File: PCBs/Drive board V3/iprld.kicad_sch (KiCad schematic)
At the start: 39 parts, among them IC4 ADS1115IDGSR, J2 Conn_01x04_Pin, U15 AMS1117-3.3, U9 TCA9548APWR

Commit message: arm, drive and power modifications
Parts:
- added H1, H2, H3, H4: MountingHole, MountingHole:MountingHole_3.2mm_M3_Pad_TopBottom, symbol Mechanical:MountingHole
- added R1: 0R, Resistor_SMD:R_0805_2012Metric, symbol Device:R
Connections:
- net +3.3V: now also R1.1
- net GND: now also CONTROL_L2.6, CONTROL_R2.6
- net GNDPWR: no longer CONTROL_L2.6, CONTROL_R2.6
- net at U2.1 (3.3V): now also R1.2
- no-connect marks 28 -> 27

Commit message: i2c breakout correction, fuck you Maciej
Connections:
- net +3.3V: now also MRS_LB1.3 (Pin_3), MRS_LF1.3 (Pin_3), MRS_RB1.3 (Pin_3), MRS_RF1.3 (Pin_3); no longer MRS_LB1.1 (Pin_1), MRS_LF1.1 (Pin_1), MRS_RB1.1 (Pin_1), MRS_RF1.1 (Pin_1)
- net SCL_LB: now also MRS_LB1.1 (Pin_1); no longer MRS_LB1.2 (Pin_2)
- net SCL_LF: now also MRS_LF1.1 (Pin_1); no longer MRS_LF1.2 (Pin_2)
- net SCL_RB: now also MRS_RB1.1 (Pin_1); no longer MRS_RB1.2 (Pin_2)
- net SCL_RF: now also MRS_RF1.1 (Pin_1); no longer MRS_RF1.2 (Pin_2)
- net SDA_LB: now also MRS_LB1.2 (Pin_2); no longer MRS_LB1.3 (Pin_3)
- net SDA_LF: now also MRS_LF1.2 (Pin_2); no longer MRS_LF1.3 (Pin_3)
- net SDA_RB: now also MRS_RB1.2 (Pin_2); no longer MRS_RB1.3 (Pin_3)
- net SDA_RF: now also MRS_RF1.2 (Pin_2); no longer MRS_RF1.3 (Pin_3)
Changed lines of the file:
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@@
 	(wire
 		(pts
+			(xy 86.36 82.55) (xy 88.9 82.55)
+		)
+		(stroke
+			(width 0)
+			(type default)
+		)
+	)
+	(wire
+		(pts
 			(xy 295.91 139.7) (xy 306.07 139.7)
 		)
@@
 		)
 	)
-	(label "SCL_RB"
-		(at 90.17 110.49 180)
-		(effects
-			(font
-				(size 1.27 1.27)
-			)
-			(justify right bottom)
-		)
-	)
 	(label "SDA_RF"
 		(at 152.4 87.63 180)
@@
 		)
 	)
-	(label "SCL_RF"
-		(at 88.9 80.01 180)
-		(effects
-			(font
-				(size 1.27 1.27)
-			)
-			(justify right bottom)
-		)
-	)
 	(label "SDA"
 		(at 190.5 77.47 0)
@@
 		)
 	)
-	(label "SCL_LF"
-		(at 39.37 80.01 180)
+	(label "SDA_RB"
+		(at 90.17 110.49 180)
 		(effects
 			(font
@@
 		)
 	)
-	(label "SDA_RB"
-		(at 90.17 113.03 180)
-		(effects
-			(font
-				(size 1.27 1.27)
-			)
-			(justify right bottom)
-		)
-	)
 	(label "I_OUT_L"
 		(at 334.01 22.86 90)
@@
 		)
 	)
-	(label "IN2_L"
-		(at 72.39 260.35 0)
-		(effects
-			(font
-				(size 1.27 1.27)
-			)
-			(justify left bottom)
-		)
-	)
-	(label "D4"
-		(at 327.66 241.3 180)
+	(label "SCL_LF"
+		(at 39.37 77.47 180)
 		(effects
 			(font
@@
 		)
 	)
-	(label "SDA_RF"
-		(at 88.9 82.55 180)
+	(label "IN2_L"
+		(at 72.39 260.35 0)
 		(effects
 			(font
 				(size 1.27 1.27)
 			)
-			(justify right bottom)
+			(justify left bottom)
 		)
 	)
-	(label "SDA_LB"
-		(at 39.37 114.3 180)
+	(label "D4"
+		(at 327.66 241.3 180)
 		(effects
 			(font
@@
 		)
 	)
+	(label "SCL_RF"
+		(at 88.9 77.47 180)
+		(effects
+			(font
+				(size 1.27 1.27)
+			)
+			(justify right bottom)
+		)
+	)
 	(label "D5"
 		(at 219.71 228.6 0)
@@
 		)
 	)
+	(label "SCL_RB"
+		(at 90.17 107.95 180)
+		(effects
+			(font
+				(size 1.27 1.27)
+			)
+			(justify right bottom)
+		)
+	)
 	(label "EN_R"
 		(at 44.45 317.5 180)
@@
 		)
 	)
+	(label "SDA_RF"
+		(at 88.9 80.01 180)
+		(effects
+			(font
+				(size 1.27 1.27)
+			)
+			(justify right bottom)
+		)
+	)
 	(label "IN2_L"
 		(at 327.66 233.68 180)
@@
 		)
 	)
-	(label "SDA_LF"
-		(at 39.37 82.55 180)
-		(effects
-			(font
-				(size 1.27 1.27)
-			)
-			(justify right bottom)
-		)
-	)
 	(label "PWM_L"
 		(at 363.22 233.68 0)
@@
 		)
 	)
+	(label "SDA_LF"
+		(at 39.37 80.01 180)
+		(effects
+			(font
+				(size 1.27 1.27)
+			)
+			(justify right bottom)
+		)
+	)
 	(label "SDA_LB"
 		(at 152.4 82.55 180)
@@
 		)
 	)
+	(label "SCL_LB"
+		(at 39.37 109.22 180)
+		(effects
+			(font
+				(size 1.27 1.27)
+			)
+			(justify right bottom)
+		)
+	)
 	(label "SCL"
 		(at 363.22 218.44 0)
@@
 		)
 	)
-	(label "SCL_LB"
+	(label "SDA_LB"
 		(at 39.37 111.76 180)
 		(effects
@@
 	(symbol
 		(lib_id "power:+3.3V")
-		(at 90.17 107.95 0)
+		(at 90.17 113.03 90)
 		(unit 1)
 		(exclude_from_sim no)
@@
 		(fields_autoplaced yes)
 		(property "Reference" "#PWR076"
-			(at 90.17 111.76 0)
+			(at 93.98 113.03 0)
 			(effects
 				(font
@@
 		)
 		(property "Value" "+3.3V"
-			(at 90.17 102.87 0)
+			(at 88.9 110.49 90)
 			(effects
 				(font
@@
 		)
 		(property "Footprint" ""
-			(at 90.17 107.95 0)
+			(at 90.17 113.03 0)
 			(effects
 				(font
@@
 		)
 		(property "Datasheet" ""
-			(at 90.17 107.95 0)
+			(at 90.17 113.03 0)
 			(effects
 				(font
@@
 		)
 		(property "Description" "Power symbol creates a global label with name \"+3.3V\""
-			(at 90.17 107.95 0)
+			(at 90.17 113.03 0)
 			(effects
 				(font
@@
 	(symbol
 		(lib_id "power:+3.3V")
-		(at 39.37 109.22 0)
+		(at 39.37 114.3 90)
 		(unit 1)
 		(exclude_from_sim no)
@@
 		(fields_autoplaced yes)
 		(property "Reference" "#PWR0101"
-			(at 39.37 113.03 0)
+			(at 43.18 114.3 0)
 			(effects
 				(font
@@
 		)
 		(property "Value" "+3.3V"
-			(at 39.37 104.14 0)
+			(at 38.1 111.76 90)
 			(effects
 				(font
@@
 		)
 		(property "Footprint" ""
-			(at 39.37 109.22 0)
+			(at 39.37 114.3 0)
 			(effects
 				(font
@@
 		)
 		(property "Datasheet" ""
-			(at 39.37 109.22 0)
+			(at 39.37 114.3 0)
 			(effects
 				(font
@@
 		)
 		(property "Description" "Power symbol creates a global label with name \"+3.3V\""
-			(at 39.37 109.22 0)
+			(at 39.37 114.3 0)
 			(effects
 				(font
@@
 	(symbol
 		(lib_id "power:+3.3V")
-		(at 88.9 77.47 0)
+		(at 86.36 82.55 90)
 		(unit 1)
 		(exclude_from_sim no)
@@
 		(fields_autoplaced yes)
 		(property "Reference" "#PWR067"
-			(at 88.9 81.28 0)
+			(at 90.17 82.55 0)
 			(effects
 				(font
@@
 		)
 		(property "Value" "+3.3V"
-			(at 88.9 72.39 0)
+			(at 85.09 80.01 90)
 			(effects
 				(font
@@
 		)
 		(property "Footprint" ""
-			(at 88.9 77.47 0)
+			(at 86.36 82.55 0)
 			(effects
 				(font
@@
 		)
 		(property "Datasheet" ""
-			(at 88.9 77.47 0)
+			(at 86.36 82.55 0)
 			(effects
 				(font
@@
 		)
 		(property "Description" "Power symbol creates a global label with name \"+3.3V\""
-			(at 88.9 77.47 0)
+			(at 86.36 82.55 0)
 			(effects
 				(font
@@
 	(symbol
 		(lib_id "power:+3.3V")
-		(at 39.37 77.47 0)
+		(at 39.37 82.55 90)
 		(unit 1)
 		(exclude_from_sim no)
@@
 		(fields_autoplaced yes)
 		(property "Reference" "#PWR07"
-			(at 39.37 81.28 0)
+			(at 43.18 82.55 0)
 			(effects
 				(font
@@
 		)
 		(property "Value" "+3.3V"
-			(at 39.37 72.39 0)
+			(at 38.1 80.01 90)
 			(effects
 				(font
@@
 		)
 		(property "Footprint" ""
-			(at 39.37 77.47 0)
+			(at 39.37 82.55 0)
 			(effects
 				(font
@@
 		)
 		(property "Datasheet" ""
-			(at 39.37 77.47 0)
+			(at 39.37 82.55 0)
 			(effects
 				(font
@@
 		)
 		(property "Description" "Power symbol creates a global label with name \"+3.3V\""
-			(at 39.37 77.47 0)
+			(at 39.37 82.55 0)
 			(effects
 				(font

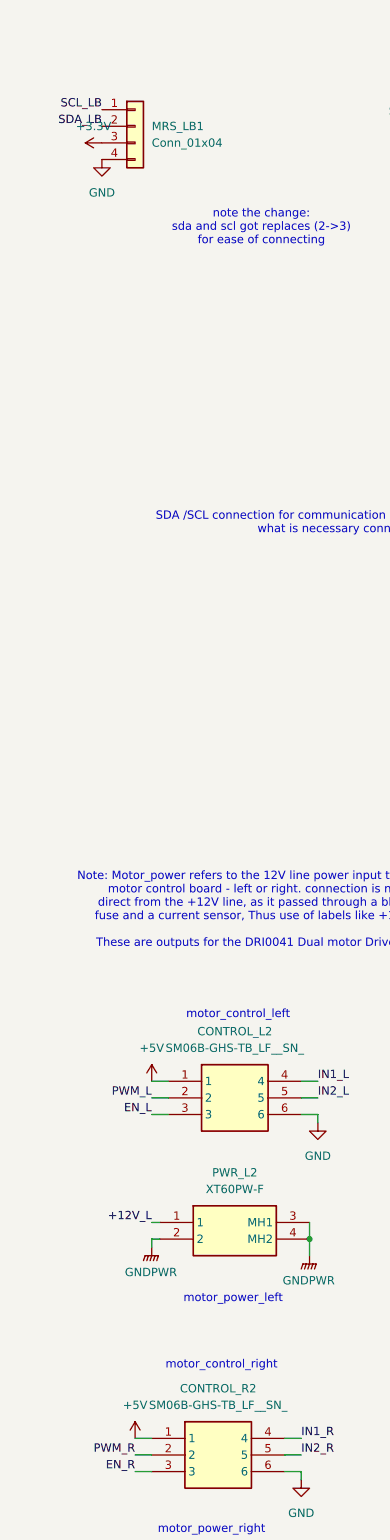
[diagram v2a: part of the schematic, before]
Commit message: changed motor reference to 3.3v
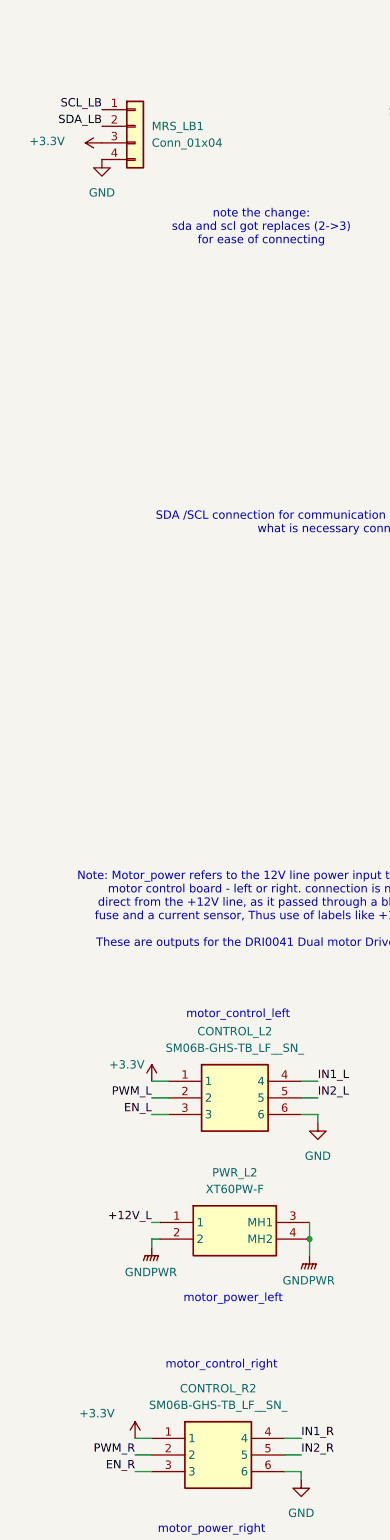
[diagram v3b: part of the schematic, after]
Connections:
- net +3.3V: now also CONTROL_L2.1, CONTROL_R2.1
- net +5V: no longer CONTROL_L2.1, CONTROL_R2.1
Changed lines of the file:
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@@
 	(symbol
 		(lib_id "power:+5V")
-		(at 46.99 257.81 0)
-		(unit 1)
-		(exclude_from_sim no)
-		(in_bom yes)
-		(on_board yes)
-		(dnp no)
-		(fields_autoplaced yes)
-		(property "Reference" "#PWR04"
-			(at 46.99 261.62 0)
-			(effects
-				(font
-					(size 1.27 1.27)
-				)
-				(hide yes)
-			)
-		)
-		(property "Value" "+5V"
-			(at 46.99 252.73 0)
-			(effects
-				(font
-					(size 1.27 1.27)
-				)
-			)
-		)
-		(property "Footprint" ""
-			(at 46.99 257.81 0)
-			(effects
-				(font
-					(size 1.27 1.27)
-				)
-				(hide yes)
-			)
-		)
-		(property "Datasheet" ""
-			(at 46.99 257.81 0)
-			(effects
-				(font
-					(size 1.27 1.27)
-				)
-				(hide yes)
-			)
-		)
-		(property "Description" "Power symbol creates a global label with name \"+5V\""
-			(at 46.99 257.81 0)
-			(effects
-				(font
-					(size 1.27 1.27)
-				)
-				(hide yes)
-			)
-		)
-		(pin "1"
-		)
-		(instances
-			(project "iprld"
-				(path "/f88582ba-beb9-4fb5-aa18-f7c4bf4c6866"
-					(reference "#PWR04")
-					(unit 1)
-				)
-			)
-		)
-	)
-	(symbol
-		(lib_id "power:+5V")
 		(at 219.71 223.52 0)
 		(unit 1)
@@
 	)
 	(symbol
-		(lib_id "power:+5V")
-		(at 44.45 312.42 0)
+		(lib_id "power:+3.3V")
+		(at 46.99 257.81 0)
 		(unit 1)
 		(exclude_from_sim no)
@@
 		(on_board yes)
 		(dnp no)
-		(fields_autoplaced yes)
-		(property "Reference" "#PWR05"
-			(at 44.45 316.23 0)
+		(property "Reference" "#PWR0105"
+			(at 46.99 261.62 0)
 			(effects
 				(font
@@
 			)
 		)
-		(property "Value" "+5V"
-			(at 44.45 307.34 0)
+		(property "Value" "+3.3V"
+			(at 43.18 255.27 0)
 			(effects
 				(font
@@
 		)
 		(property "Footprint" ""
-			(at 44.45 312.42 0)
+			(at 46.99 257.81 0)
 			(effects
 				(font
@@
 		)
 		(property "Datasheet" ""
-			(at 44.45 312.42 0)
+			(at 46.99 257.81 0)
 			(effects
 				(font
@@
 			)
 		)
-		(property "Description" "Power symbol creates a global label with name \"+5V\""
-			(at 44.45 312.42 0)
+		(property "Description" "Power symbol creates a global label with name \"+3.3V\""
+			(at 46.99 257.81 0)
 			(effects
 				(font
@@
 			(project "iprld"
 				(path "/f88582ba-beb9-4fb5-aa18-f7c4bf4c6866"
-					(reference "#PWR05")
+					(reference "#PWR0105")
 					(unit 1)
 				)
@@
 		(on_board yes)
 		(dnp no)
-		(fields_autoplaced yes)
 		(property "Reference" "#PWR0101"
 			(at 43.18 114.3 0)
@@
 		)
 		(property "Value" "+3.3V"
-			(at 38.1 111.76 90)
+			(at 30.988 114.046 90)
 			(effects
 				(font
@@
 					(unit 1)
 				)
+			)
+		)
+	)
+	(symbol
+		(lib_id "power:+3.3V")
+		(at 44.45 312.42 0)
+		(unit 1)
+		(exclude_from_sim no)
+		(in_bom yes)
+		(on_board yes)
+		(dnp no)
+		(property "Reference" "#PWR0106"
+			(at 44.45 316.23 0)
+			(effects
+				(font
+					(size 1.27 1.27)
+				)
+				(hide yes)
+			)
+		)
+		(property "Value" "+3.3V"
+			(at 38.608 308.61 0)
+			(effects
+				(font
+					(size 1.27 1.27)
+				)
+			)
+		)
+		(property "Footprint" ""
+			(at 44.45 312.42 0)
+			(effects
+				(font
+					(size 1.27 1.27)
+				)
+				(hide yes)
+			)
+		)
+		(property "Datasheet" ""
+			(at 44.45 312.42 0)
+			(effects
+				(font
+					(size 1.27 1.27)
+				)
+				(hide yes)
+			)
+		)
+		(property "Description" "Power symbol creates a global label with name \"+3.3V\""
+			(at 44.45 312.42 0)
+			(effects
+				(font
+					(size 1.27 1.27)
+				)
+				(hide yes)
+			)
+		)
+		(pin "1"
+		)
+		(instances
+			(project "iprld"
+				(path "/f88582ba-beb9-4fb5-aa18-f7c4bf4c6866"
+					(reference "#PWR0106")
+					(unit 1)
+				)

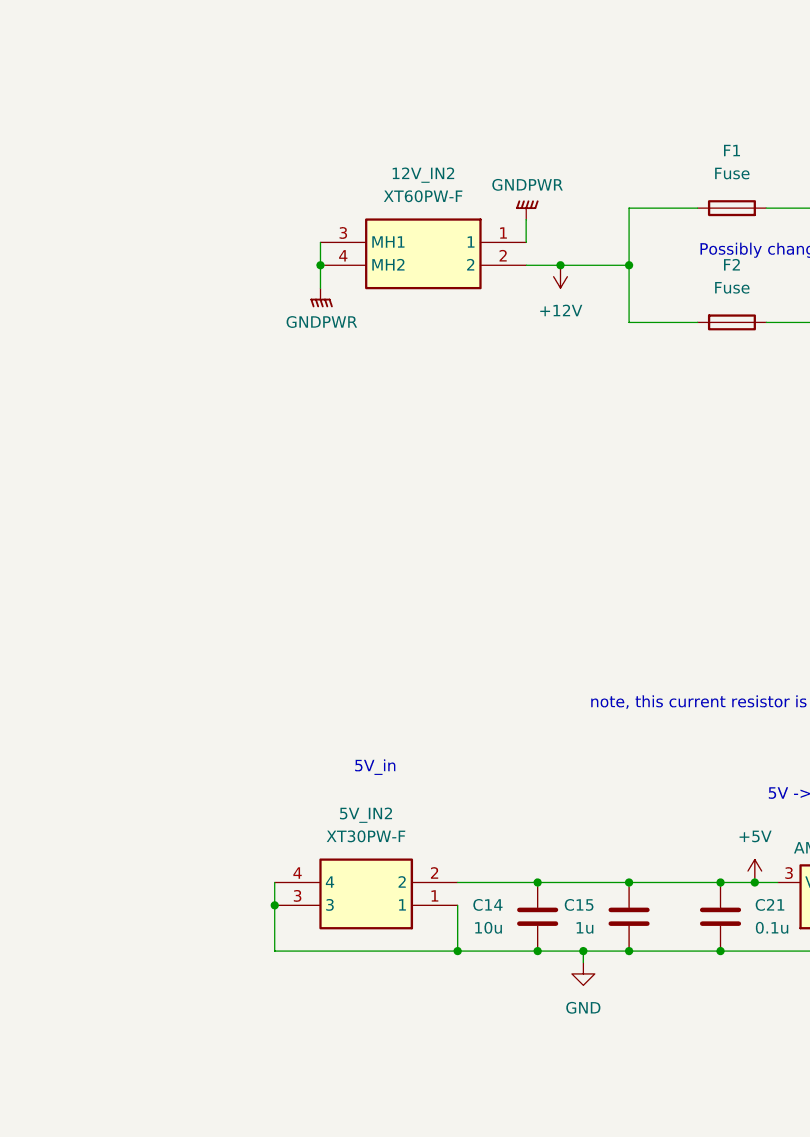
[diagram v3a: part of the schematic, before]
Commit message: David half assed the motor reference change and didnt update the layout
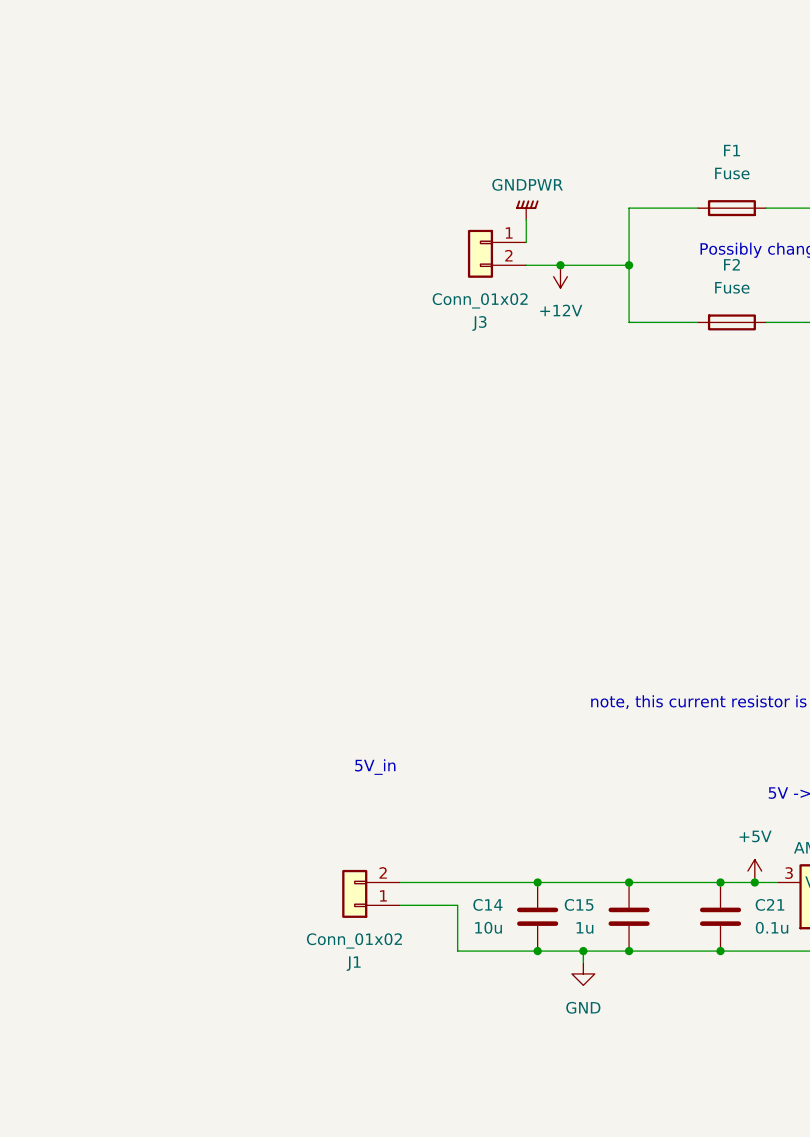
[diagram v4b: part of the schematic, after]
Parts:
- removed 12V_IN2: XT60PW-F, Connector_AMASS:AMASS_XT60PW-M_1x02_P7.20mm_Horizontal, symbol XT60PW-F:XT60PW-F
- removed 5V_IN2: XT30PW-F, Connector_AMASS:AMASS_XT30PW-M_1x02_P2.50mm_Horizontal, symbol XT30PW-F:XT30PW-F
- added J1: Conn_01x02, Connector_AMASS:AMASS_XT30PW-M_1x02_P2.50mm_Horizontal, symbol Connector_Generic:Conn_01x02
- added J3: Conn_01x02, Connector_AMASS:AMASS_XT60PW-M_1x02_P7.20mm_Horizontal, symbol Connector_Generic:Conn_01x02
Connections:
- net +12V: now also J3.2 (Pin_2)
- net +5V: now also J1.2 (Pin_2)
- net GND: now also J1.1 (Pin_1)
- net GNDPWR: now also J3.1 (Pin_1)
